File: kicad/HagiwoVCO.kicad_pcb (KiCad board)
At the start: 2 copper layers, 37.5 x 148.9 mm, 58 parts, among them J1 Conn_02x05_Counter_Clockwise, J2 ModeCV, J3 Parameter 1 CV, J4 Parameter 2 CV, J5 Gain CV, J6 V/OCT, J7 Output, SW1 SW_SPDT, U1 TL072

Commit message: tweak layout
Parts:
- RV4: value 100K -> A100K GAIN; footprint Potentiometer_THT:Potentiometer_Bourns_3266W_Vertical -> Potentiometer_THT:Potentiometer_Alps_RK09L_Single_Vertical
- moved RV4 13.3 mm to (39.6, 81.4), turned to 0 degrees
- moved J4 13.2 mm to (25.5, 58.4)
- moved RV3 13.2 mm to (39.6, 62.4)
- moved J3 6.71 mm to (25.6, 38.5)
- moved RV2 6.69 mm to (39.7, 42.4)
- moved D1 1.51 mm to (44.8, 96.4)
- moved J6 1.22 mm to (25.8, 18.5)
- moved RV1 1.22 mm to (39.9, 22.4)
- moved D5 1.03 mm to (52.4, 96.4)
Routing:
- net Net-(R3-Pad2): track 70.2 -> 0.00 mm, vias 4 -> 0
- net +12V: track 99.0 -> 169.2 mm, vias 6 -> 10
- net Net-(D1-Pad2): track 47.9 -> 49.2 mm

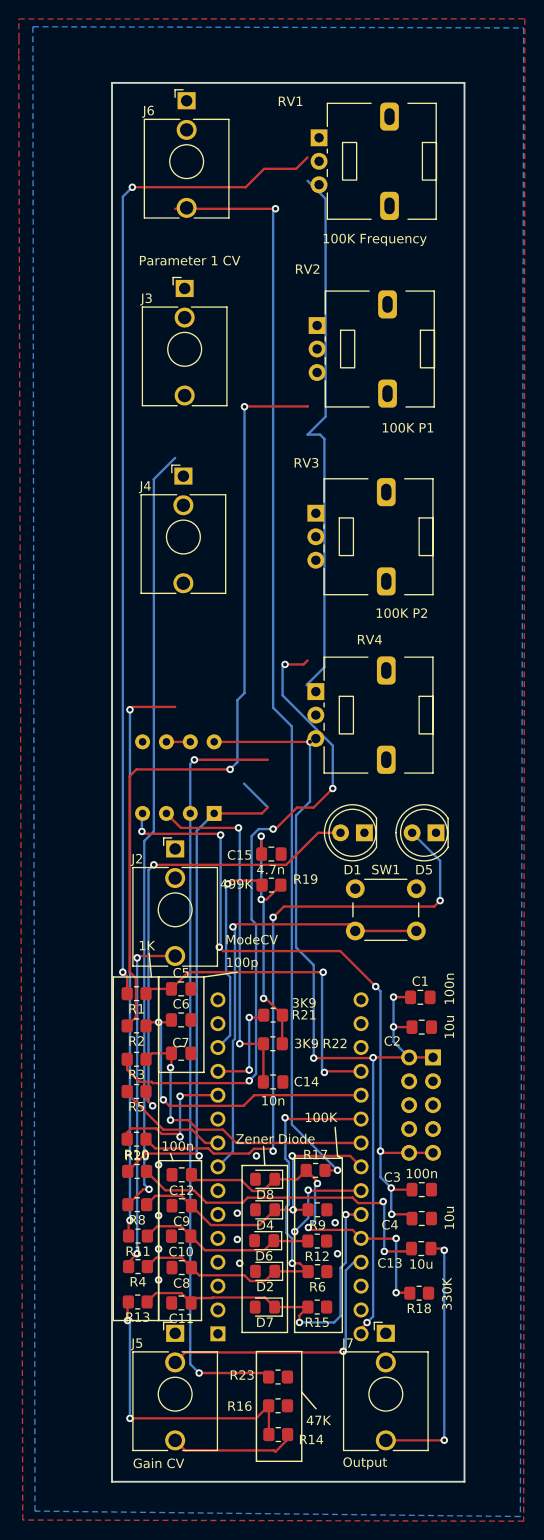
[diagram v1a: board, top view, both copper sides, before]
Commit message: routing and layout work on pcb
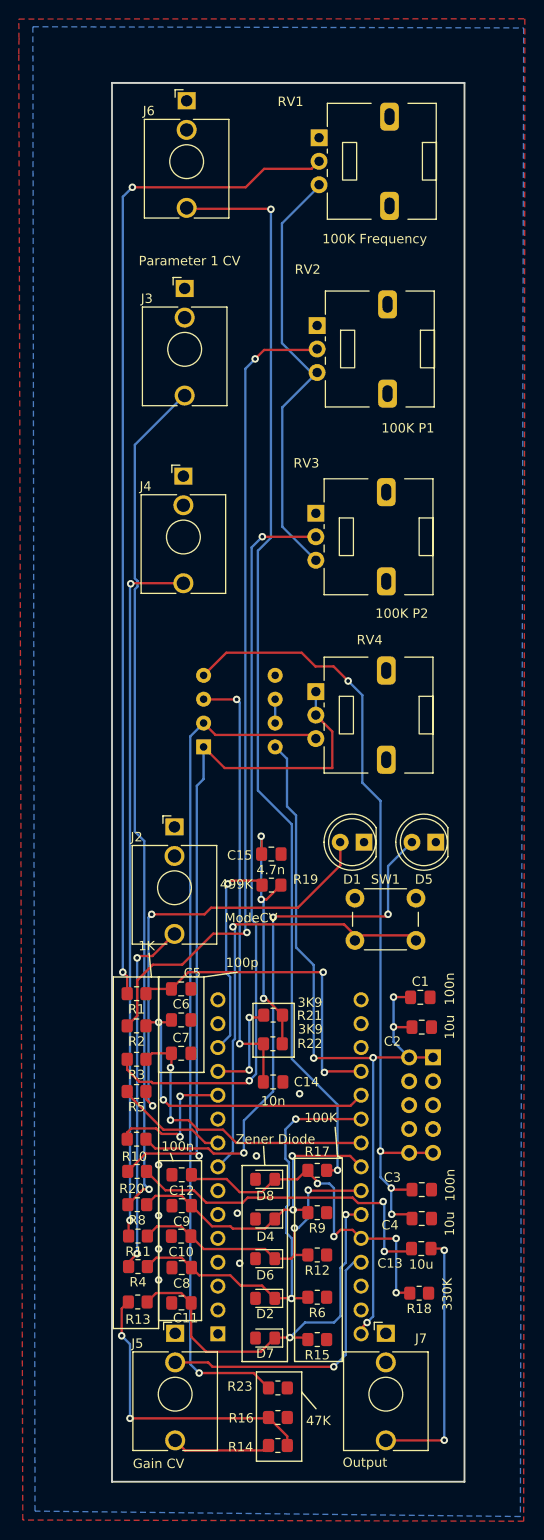
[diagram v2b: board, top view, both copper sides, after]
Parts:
- moved U1 7.17 mm to (27.6, 87.3), turned to 0 degrees
- moved R15 3.46 mm to (39.8, 150.4)
- moved D7 3.29 mm to (34.2, 150.2)
- moved D2 2.88 mm to (34.2, 146.0)
- moved R6 2.73 mm to (39.8, 145.9)
- moved J2 2.35 mm to (24.6, 95.8)
- moved D6 1.92 mm to (34.2, 141.8)
- moved R12 1.48 mm to (39.8, 141.4)
- moved R16 1.25 mm to (35.6, 158.7)
- moved R14 1.17 mm to (35.6, 161.6), turned to 180 degrees
- moved R23 1.16 mm to (35.6, 155.5)
- moved SW1 1.01 mm to (43.8, 103.4)
- moved D1 1.00 mm to (44.7, 97.4)
- moved D5 1.00 mm to (52.4, 97.4)
- moved D4 0.97 mm to (34.2, 137.5)
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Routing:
- net +12V: track 169.2 -> 88.6 mm, vias 10 -> 5
- net Net-(R3-Pad2): track 0.00 -> 79.4 mm, vias 0 -> 2
- net Net-(R20-Pad1): track 55.4 -> 75.9 mm
- net Net-(J4-PadT): track 61.0 -> 75.2 mm
- net Net-(RV1-Pad3): track 57.6 -> 46.5 mm
- net -12V: track 76.1 -> 86.6 mm, vias 7 -> 4
- net Net-(R23-Pad2): track 81.3 -> 90.8 mm, vias 2 -> 1
- net Net-(C14-Pad1): track 37.9 -> 46.9 mm
- net Net-(J3-PadT): track 82.4 -> 90.5 mm
- net Net-(D5-Pad2): track 66.3 -> 58.6 mm
- net Net-(A1-Pad25): track 37.9 -> 41.9 mm
- net Net-(R2-Pad2): track 84.2 -> 87.7 mm
- net Net-(J5-PadT): track 13.5 -> 10.6 mm
- net Net-(A1-Pad24): track 30.7 -> 32.5 mm
- net Net-(D1-Pad2): track 49.2 -> 47.8 mm
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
